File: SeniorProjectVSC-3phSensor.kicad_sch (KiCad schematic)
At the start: 49 parts, among them J1 Conn_01x15, J10 IC-, J11 UN, J2 UA, J3 UB, J4 UC, J5 IA+, J6 IA-, J7 IB+, J8 IB-, J9 IC+, U1 ATM90E32AS-AU-R, Y1 Crystal

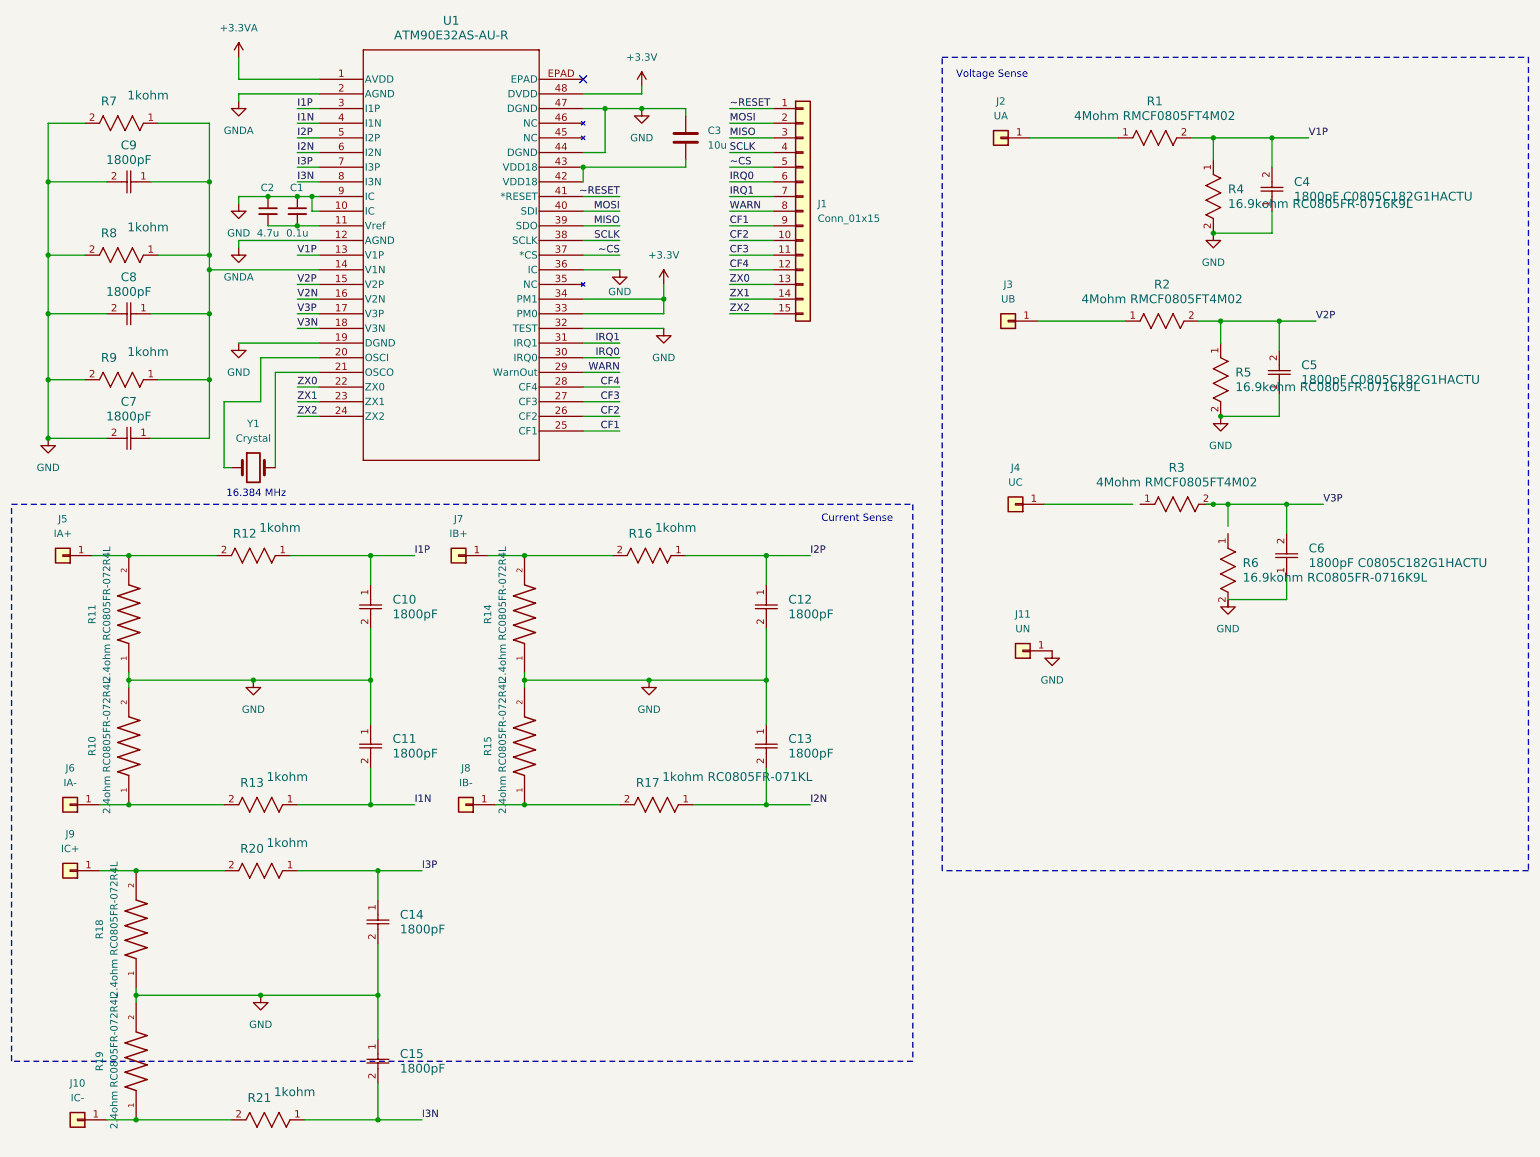
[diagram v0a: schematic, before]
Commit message: Added OSC footprint and cleaned up names.
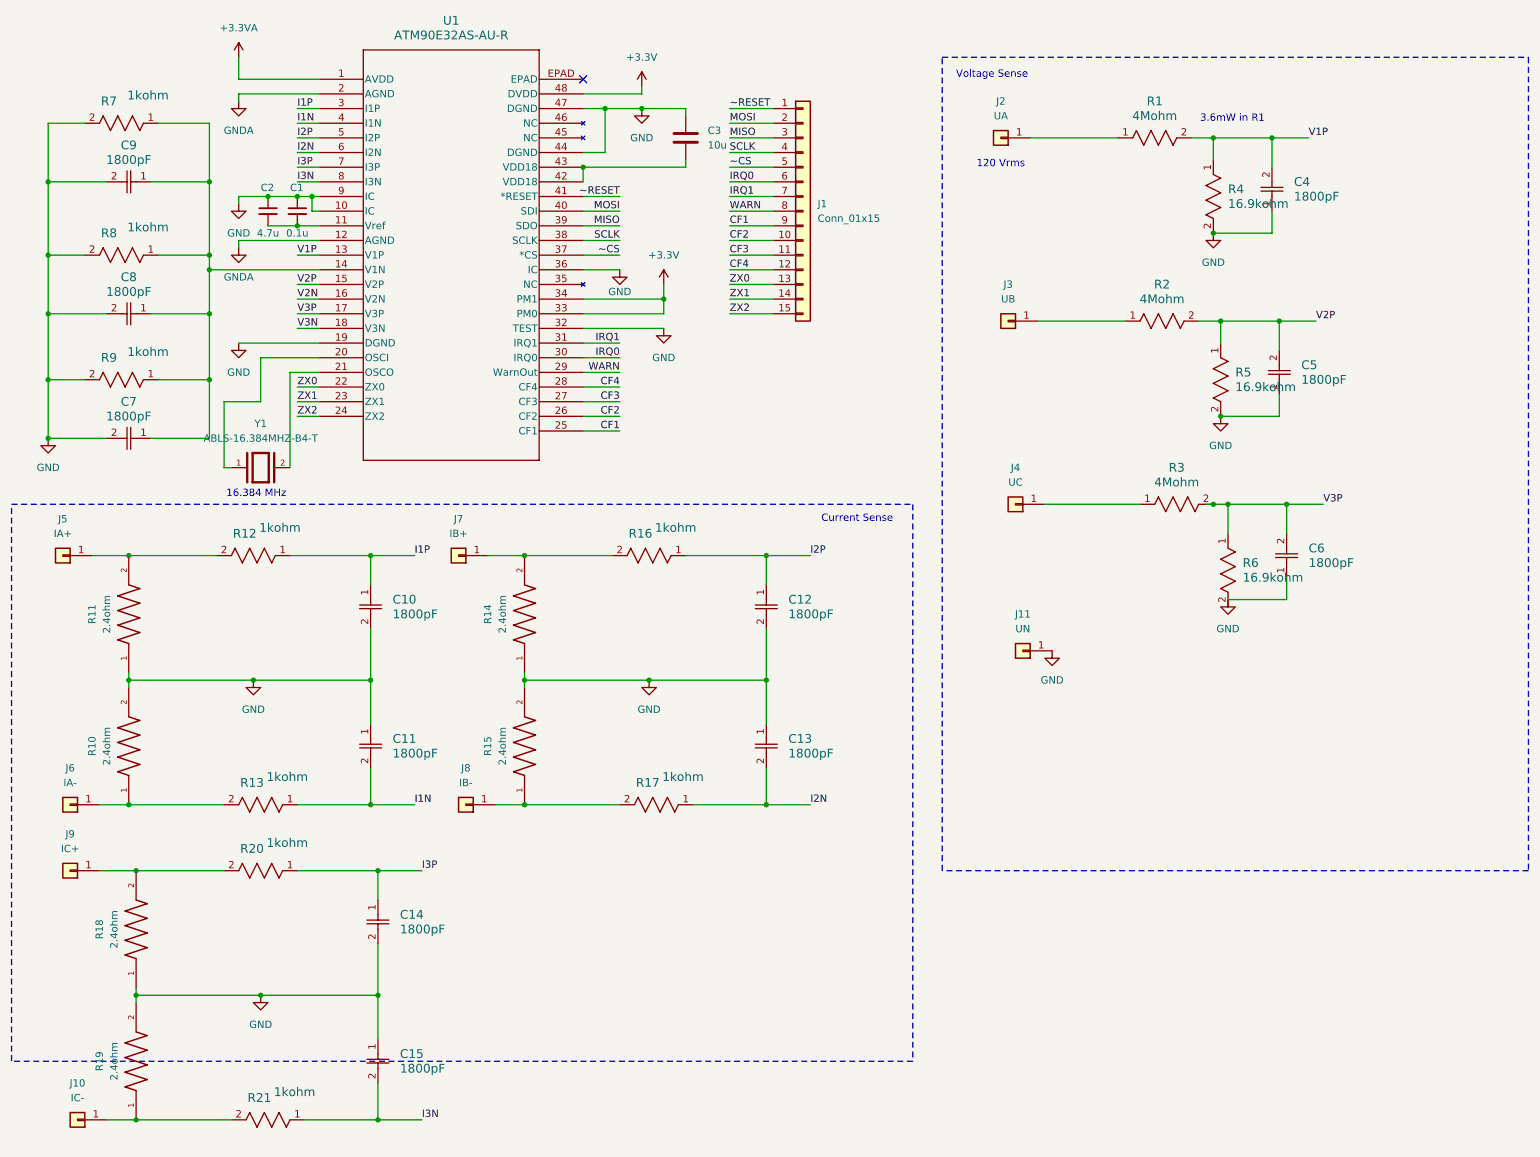
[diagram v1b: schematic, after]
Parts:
- removed Y1: Crystal, symbol Device:Crystal
- added Y1: ABLS-16.384MHZ-B4-T, Crystal:Crystal_SMD_HC49-SD_HandSoldering, symbol ABLS-16.384MHZ:ABLS-16.384MHZ-B4-T
- C1, C2, C3: footprint (none) -> Capacitor_SMD:C_0805_2012Metric_Pad1.18x1.45mm_HandSolder
- C10, C11, C12, C13, C14, C15, C7, C8, C9: footprint CAPC220145_100N_KEM -> Capacitor_SMD:C_0805_2012Metric_Pad1.18x1.45mm_HandSolder
- C4, C5, C6: value 1800pF C0805C182G1HACTU -> 1800pF; footprint CAPC220145_100N_KEM -> Capacitor_SMD:C_0805_2012Metric_Pad1.18x1.45mm_HandSolder
- R1, R2, R3: value 4Mohm RMCF0805FT4M02 -> 4Mohm; footprint RES_RMCF0805_STP -> Resistor_SMD:R_0805_2012Metric_Pad1.20x1.40mm_HandSolder
- R10, R11, R14, R15, R18, R19: value 2.4ohm RC0805FR-072R4L -> 2.4ohm; footprint RC0805FR-072R4L:RESC2012X60N -> Resistor_SMD:R_0805_2012Metric_Pad1.20x1.40mm_HandSolder
- R12, R13, R16, R20, R21, R7, R8, R9: footprint RC0805N_YAG -> Resistor_SMD:R_0805_2012Metric_Pad1.20x1.40mm_HandSolder
- R17: value 1kohm RC0805FR-071KL -> 1kohm; footprint RC0805N_YAG -> Resistor_SMD:R_0805_2012Metric_Pad1.20x1.40mm_HandSolder
- R4, R5, R6: value 16.9kohm RC0805FR-0716K9L -> 16.9kohm; footprint RC0805N_YAG -> Resistor_SMD:R_0805_2012Metric_Pad1.20x1.40mm_HandSolder
- U1: footprint TQFP48_7x7MC_MCH -> ATM90E3:TQFP48_7x7MC_MCH
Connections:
- net V3P: now also R6.1
- net at U1.20 (OSCI): now also Y1.1
- net at U1.21 (OSCO): now also Y1.2
- net at R3.1: now also J4.1 (Pin_1)
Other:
- note added: "120 Vrms"
- note added: "3.6mW in R1"
